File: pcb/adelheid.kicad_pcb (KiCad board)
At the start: 2 copper layers, 339.1 x 143.2 mm, 323 parts, among them J1 USB_B_Mini, J12 VCC, J13 D+, J14 D-, J15 GND, J2 MISO, J3 VCC, J4 SCK, J5 MOSI, J6 RES, J7 GND, J8 PF4, J9 PF5, Q1 2N7002, U1 USBLC6-2SC6, U2 ATmega32U4-AU, Y1 Crystal_GND24

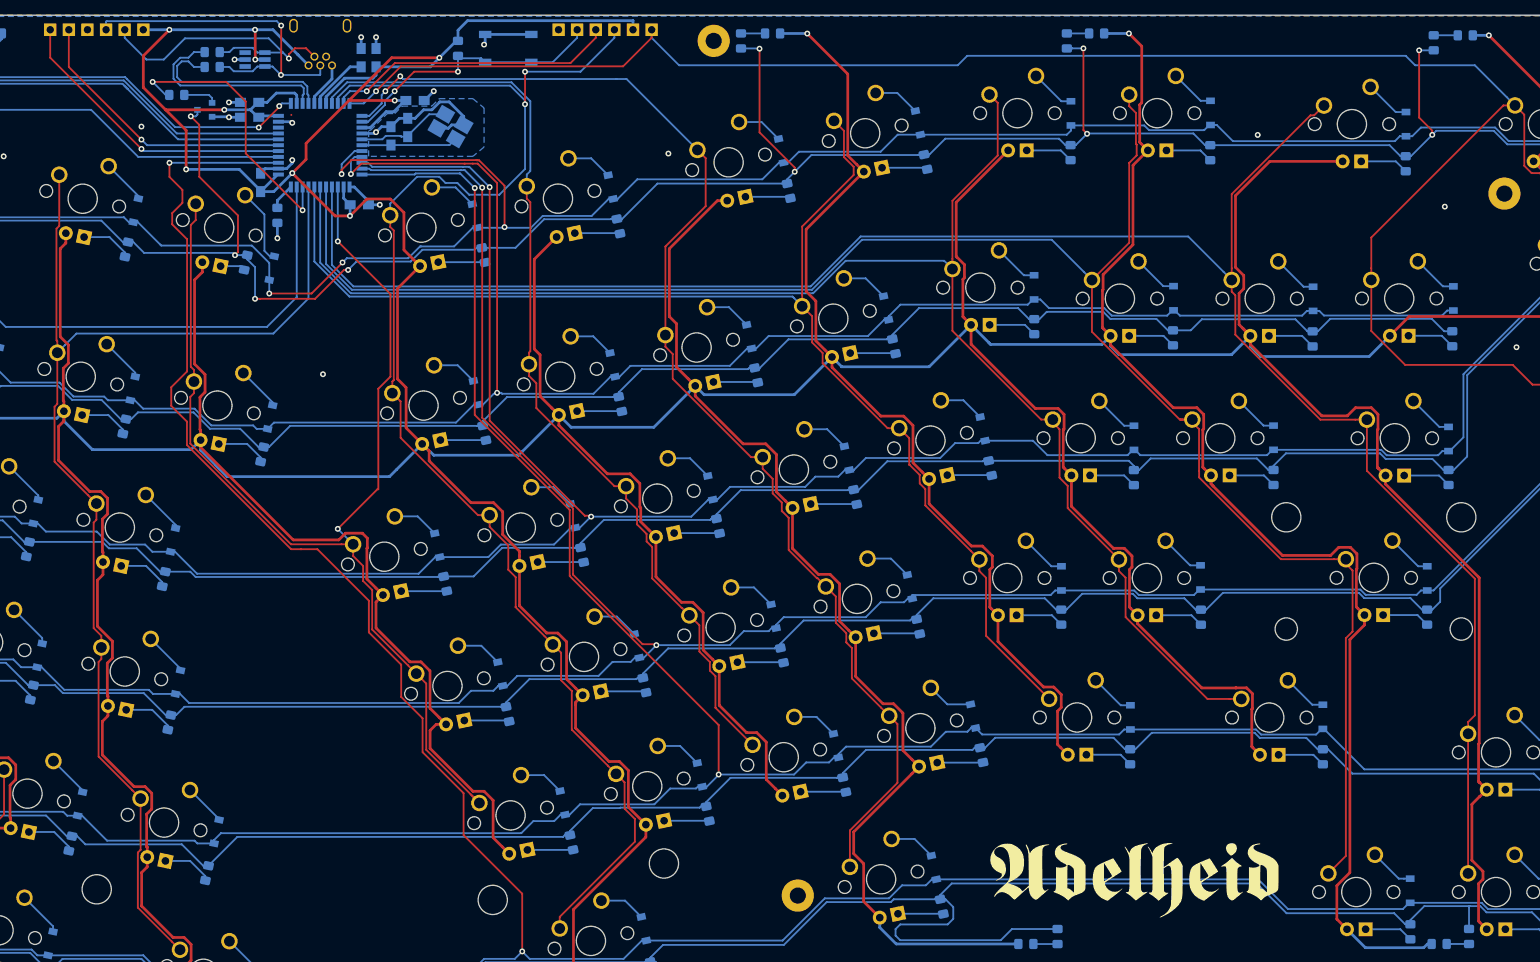
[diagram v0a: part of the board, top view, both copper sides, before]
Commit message: added rotary
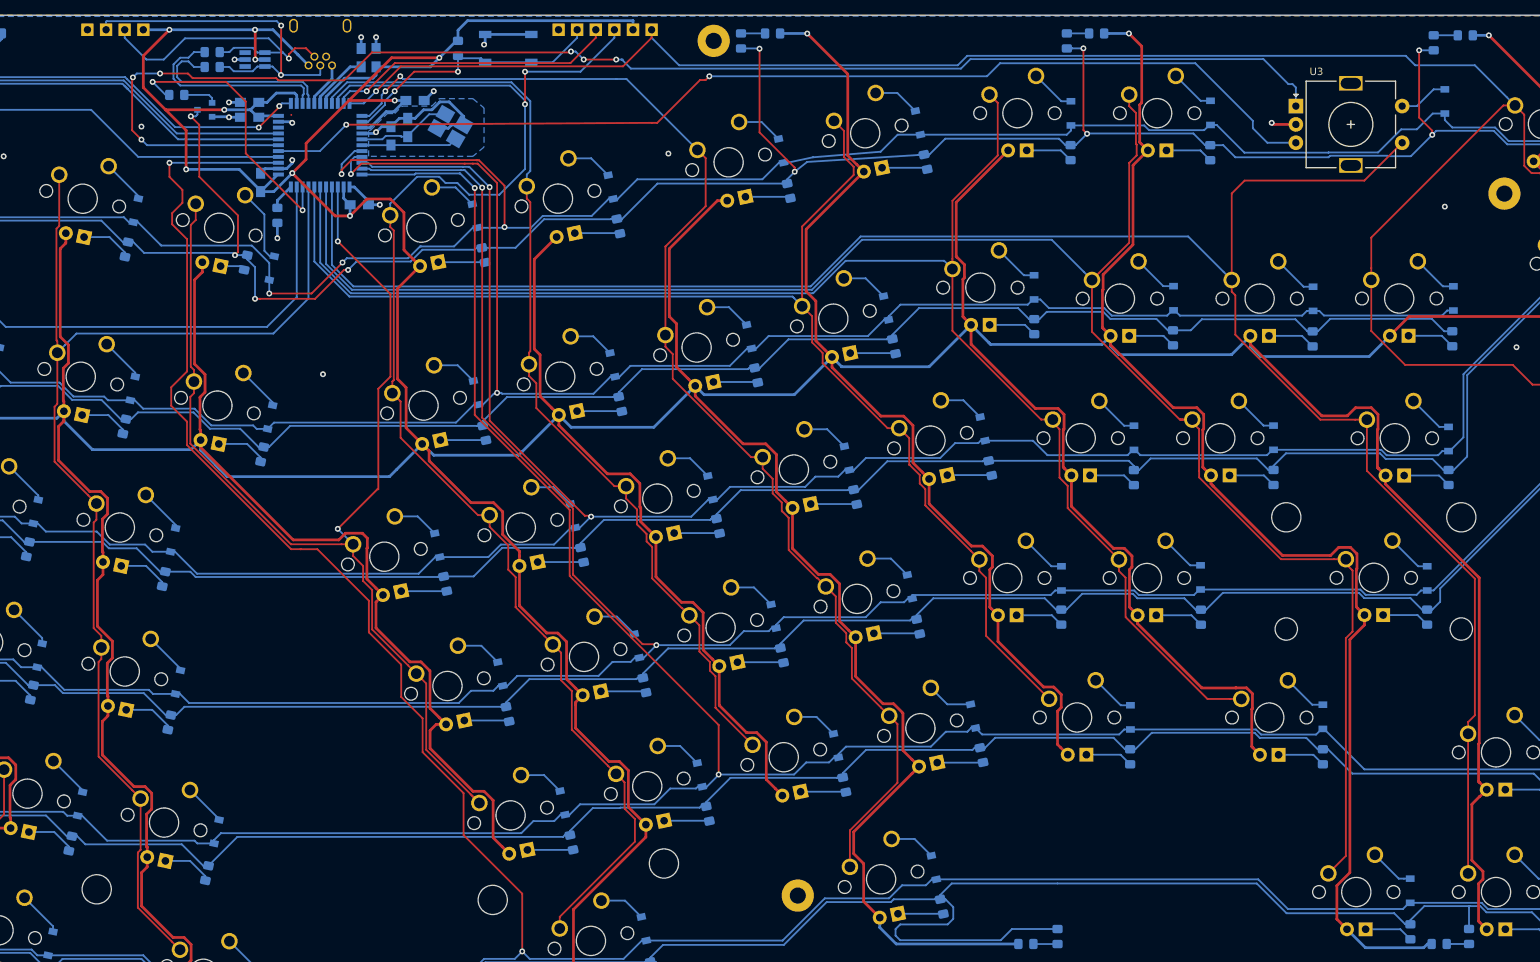
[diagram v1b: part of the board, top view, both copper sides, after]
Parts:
- removed  G2: LOGO, adelheid:adelheid-logo
- removed G1: LOGO, adelheid:adelheid-logo
- removed J8: PF4, Pin_Headers:Pin_Header_Straight_1x01_Pitch2.54mm
- removed J9: PF5, Pin_Headers:Pin_Header_Straight_1x01_Pitch2.54mm
- removed MX72: MX-LED, ai03-MX_only:MXOnly-1U
- removed RL72: R, Resistor_SMD:R_0805_2012Metric_Pad1.15x1.40mm_HandSolder
- added U3: rotary_encoder, encoder:RotaryEncoder_Alps_EC11E-Switch_Vertical_H20mm, F.Cu at (308.6, 36.8)
- moved D72 6.14 mm to (328.9, 36.2)
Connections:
- D72 pad 2: Net-(D72-Pad2) -> (no net)
- J1 pad 4: Net-(J1-Pad4) -> (no net)
- U1 pad 1: Net-(U1-Pad1) -> (no net)
- U1 pad 3: Net-(U1-Pad3) -> (no net)
- U2 pad 38: /PF5 -> (no net)
- U2 pad 39: /PF4 -> (no net)
- U2 pad 42: Net-(U2-Pad42) -> (no net)
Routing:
- net (no net): track 0.00 -> 350.2 mm, vias 0 -> 8
- net /PF5: track 40.2 -> 0.00 mm, vias 1 -> 0
- net VCC: track 2646.7 -> 2608.2 mm
- net /PF4: track 38.1 -> 0.00 mm, vias 1 -> 0
- net /col13: track 268.0 -> 276.6 mm
- net Net-(MX72-Pad4): track 6.63 -> 0.00 mm
- net Net-(D72-Pad2): track 6.26 -> 0.00 mm
- net GND: track 61.7 -> 65.0 mm
- net /row0: track 367.0 -> 369.9 mm
